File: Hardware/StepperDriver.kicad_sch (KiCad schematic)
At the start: 59 parts, among them J1 DC, J2 MOTOR, J3 OLED, J4 JTAG, SW1 SPST_TS, SW2 SPST_TS, SW3 SPST_TS, U1 TPS5430DDA, U2 TMC2208-LA, U3 XIAO-ESP32C6

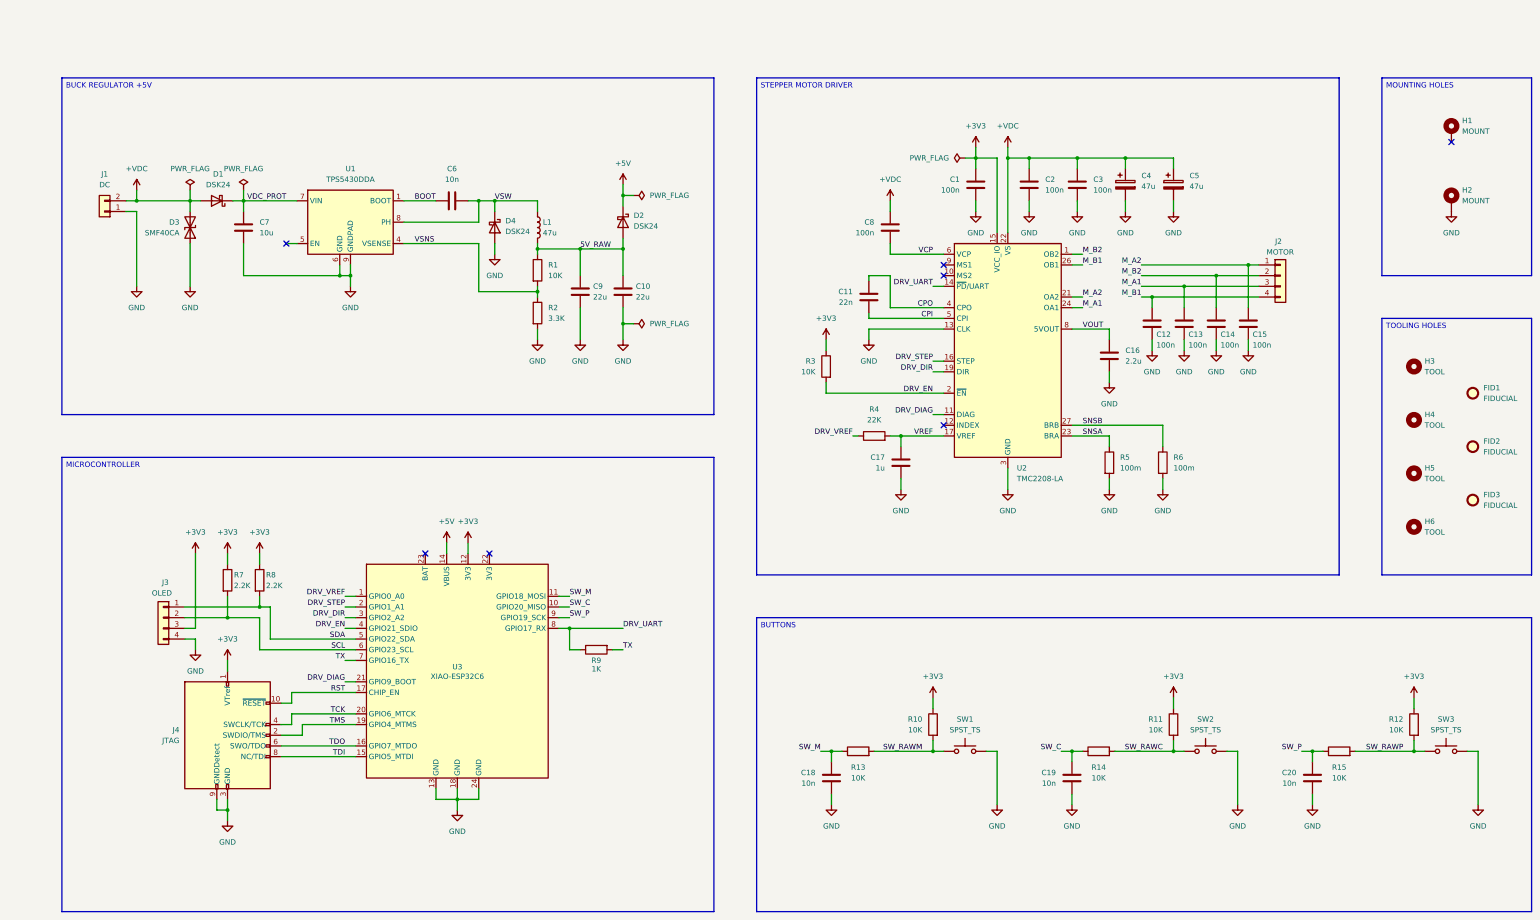
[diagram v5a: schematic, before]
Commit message: Driver update
Moved to the better TMC2209 stepper motor driver.
Added a status LED for the voltage regulator.
Updated the output files.
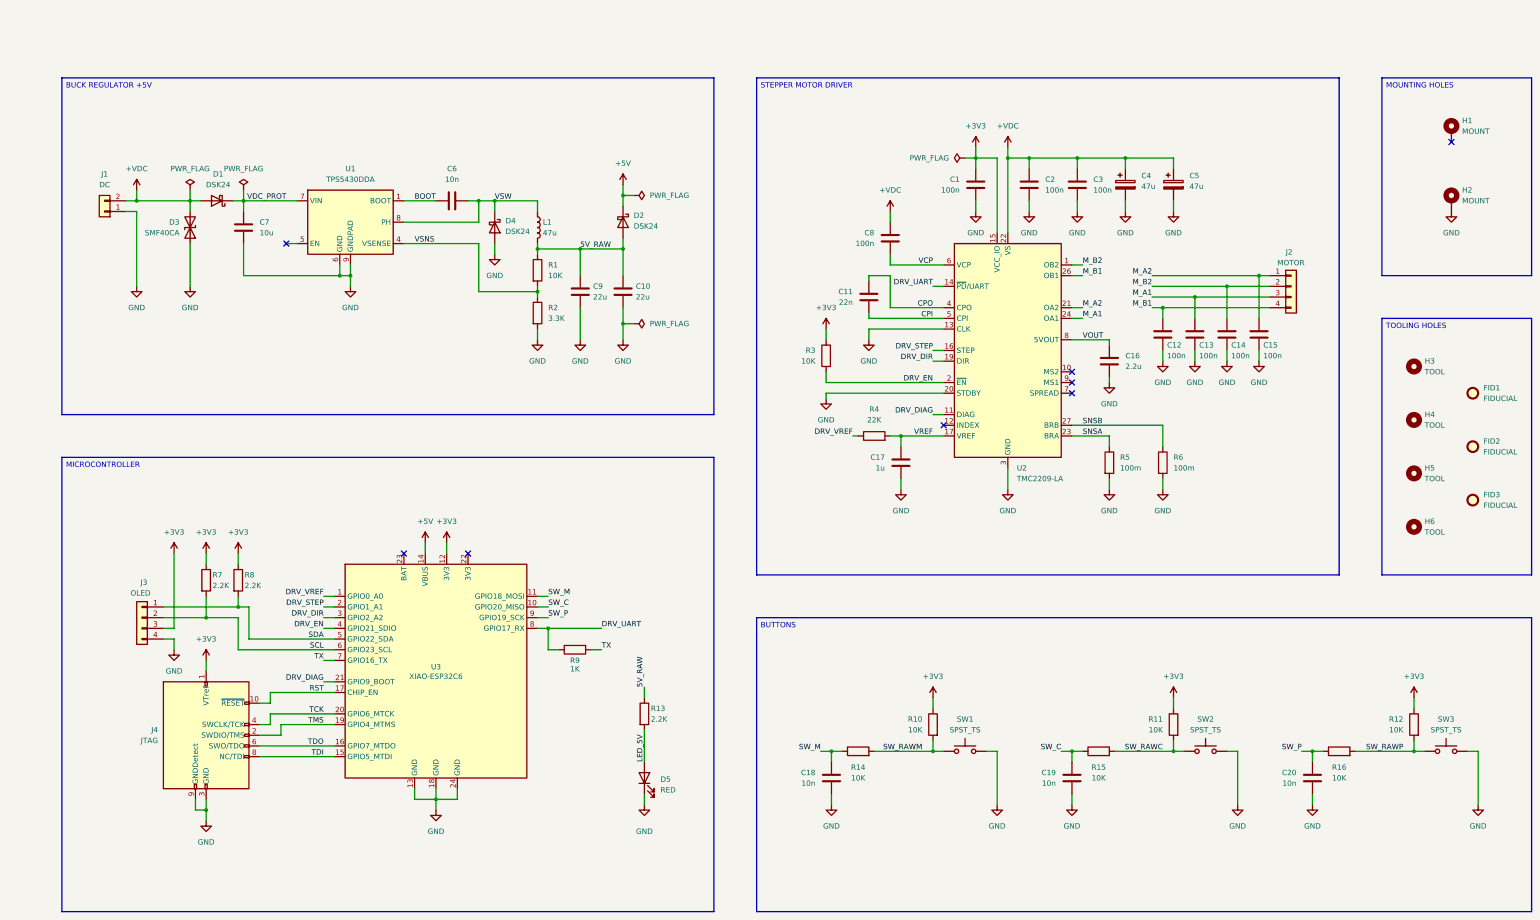
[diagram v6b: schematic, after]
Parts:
- removed U2: TMC2208-LA, Custom_Parts:QFN-28-1EP_5x5mm_P0.5mm_EP3.1x3.1mm_ThermalVias, symbol Driver_Motor:TMC2208-LA
- added D5: RED, LED_SMD:LED_0603_1608Metric, symbol Device:LED
- added R13: 2.2K, Resistor_SMD:R_0603_1608Metric, symbol Device:R
- added U2: TMC2209-LA, Custom_Parts:VQFN-28-1EP_5x5mm_P0.5mm_EP3.7x3.7mm_ThermalVias, symbol Custom_Parts:TMC2209-LA
- renumbered R13 to R14, R14 to R15, R15 to R16
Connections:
- net +3V3: now also U2.15 (VCC_IO)
- net +VDC: now also U2.22 (VS), U2.28 (VS)
- net 5V_RAW: now also R13.1
- net CPI: now also U2.5 (CPI)
- net CPO: now also U2.4 (CPO)
- net DRV_DIAG: now also U2.11 (DIAG)
- net DRV_DIR: now also U2.19 (DIR)
- net DRV_EN: now also U2.2 (~{EN})
- net DRV_STEP: now also U2.16 (STEP)
- net DRV_UART: now also U2.14 (~{PD}/UART)
- net GND: now also D5.1 (K), U2.13 (CLK), U2.18 (GND), U2.20 (STDBY), U2.29 (GND), U2.3 (GND)
- net M_A1: now also U2.24 (OA1)
- net M_A2: now also U2.21 (OA2)
- net M_B1: now also U2.26 (OB1)
- net M_B2: now also U2.1 (OB2)
- net SNSA: now also U2.23 (BRA)
- net SNSB: now also U2.27 (BRB)
- net VCP: now also U2.6 (VCP)
- net VOUT: now also U2.8 (5VOUT)
- net VREF: now also U2.17 (VREF)
- new net LED_5V: D5.2 (A), R13.2
- no-connect marks 7 -> 8
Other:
- moved on the sheet: C12, C13, C14, C15, C16, C8, J2, J3, J4, R3, R7, R8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

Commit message: Output files
Minor changes on the PCB.
Updated the bulk capacitors for the board to have a lower voltage rating.
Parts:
- C4, C5: footprint Capacitor_SMD:CP_Elec_6.3x5.4 -> Capacitor_SMD:CP_Elec_6.3x5.8; JLCPCB Part C44606723 -> C5246552; Manufacturer Part SM476M050E0800 -> HV1V476M0605PZ
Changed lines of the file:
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@@
 			)
 		)
-		(property "Footprint" "Capacitor_SMD:CP_Elec_6.3x5.4"
+		(property "Footprint" "Capacitor_SMD:CP_Elec_6.3x5.8"
 			(at 286.7152 66.04 0)
 			(hide yes)
@@
 			)
 		)
-		(property "JLCPCB Part" "C44606723"
+		(property "JLCPCB Part" "C5246552"
 			(at 285.75 62.23 0)
 			(hide yes)
@@
 			)
 		)
-		(property "Manufacturer Part" "SM476M050E0800"
+		(property "Manufacturer Part" "HV1V476M0605PZ"
 			(at 285.75 62.23 0)
 			(hide yes)
@@
 			)
 		)
-		(property "Footprint" "Capacitor_SMD:CP_Elec_6.3x5.4"
+		(property "Footprint" "Capacitor_SMD:CP_Elec_6.3x5.8"
 			(at 298.1452 66.04 0)
 			(hide yes)
@@
 			)
 		)
-		(property "JLCPCB Part" "C44606723"
+		(property "JLCPCB Part" "C5246552"
 			(at 297.18 62.23 0)
 			(hide yes)
@@
 			)
 		)
-		(property "Manufacturer Part" "SM476M050E0800"
+		(property "Manufacturer Part" "HV1V476M0605PZ"
 			(at 297.18 62.23 0)
 			(hide yes)

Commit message: Output files
Minor changes to the board and schematic.
Updated the output files.
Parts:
- removed H4: TOOL, MountingHole:ToolingHole_1.152mm, symbol Mechanical:MountingHole
- R9: value 1K -> 0R; JLCPCB Part C21190 -> C21189; Manufacturer Part 0603WAF1001T5E -> 0603WAF0000T5E
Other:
- moved on the sheet: FID1, FID3, H3, H5, H6
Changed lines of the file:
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@@
 	(symbol
 		(lib_id "Mechanical:MountingHole")
-		(at 354.33 130.81 0)
+		(at 354.33 124.46 0)
 		(unit 1)
 		(body_style 1)
@@
 		(fields_autoplaced yes)
 		(property "Reference" "H5"
-			(at 356.87 129.5399 0)
+			(at 356.87 123.1899 0)
 			(show_name no)
 			(do_not_autoplace no)
@@
 		)
 		(property "Value" "TOOL"
-			(at 356.87 132.0799 0)
+			(at 356.87 125.7299 0)
 			(show_name no)
 			(do_not_autoplace no)
@@
 		)
 		(property "Footprint" "MountingHole:ToolingHole_1.152mm"
-			(at 354.33 130.81 0)
+			(at 354.33 124.46 0)
 			(hide yes)
 			(show_name no)
@@
 		)
 		(property "Datasheet" ""
-			(at 354.33 130.81 0)
+			(at 354.33 124.46 0)
 			(hide yes)
 			(show_name no)
@@
 		)
 		(property "Description" "Mounting Hole without connection"
-			(at 354.33 130.81 0)
+			(at 354.33 124.46 0)
 			(hide yes)
 			(show_name no)
@@
 		)
 		(property "JLCPCB Part" "-"
-			(at 354.33 130.81 0)
+			(at 354.33 124.46 0)
 			(hide yes)
 			(show_name no)
@@
 		)
 		(property "Manufacturer Part" "-"
-			(at 354.33 130.81 0)
+			(at 354.33 124.46 0)
 			(hide yes)
 			(show_name no)
@@
 	(symbol
 		(lib_id "Mechanical:MountingHole")
-		(at 354.33 105.41 0)
+		(at 354.33 107.95 0)
 		(unit 1)
 		(body_style 1)
@@
 		(fields_autoplaced yes)
 		(property "Reference" "H3"
-			(at 356.87 104.1399 0)
-			(show_name no)
-			(do_not_autoplace no)
-			(effects
-				(font
-					(size 1.27 1.27)
-				)
-				(justify left)
-			)
-		)
-		(property "Value" "TOOL"
 			(at 356.87 106.6799 0)
 			(show_name no)
@@
 			)
 		)
-		(property "Footprint" "MountingHole:ToolingHole_1.152mm"
-			(at 354.33 105.41 0)
-			(hide yes)
-			(show_name no)
-			(do_not_autoplace no)
-			(effects
-				(font
-					(size 1.27 1.27)
-				)
-			)
-		)
-		(property "Datasheet" ""
-			(at 354.33 105.41 0)
-			(hide yes)
-			(show_name no)
-			(do_not_autoplace no)
-			(effects
-				(font
-					(size 1.27 1.27)
-				)
-			)
-		)
-		(property "Description" "Mounting Hole without connection"
-			(at 354.33 105.41 0)
-			(hide yes)
-			(show_name no)
-			(do_not_autoplace no)
-			(effects
-				(font
-					(size 1.27 1.27)
-				)
-			)
-		)
-		(property "JLCPCB Part" "-"
-			(at 354.33 105.41 0)
-			(hide yes)
-			(show_name no)
-			(do_not_autoplace no)
-			(effects
-				(font
-					(size 1.27 1.27)
-				)
-			)
-		)
-		(property "Manufacturer Part" "-"
-			(at 354.33 105.41 0)
-			(hide yes)
-			(show_name no)
-			(do_not_autoplace no)
-			(effects
-				(font
-					(size 1.27 1.27)
-				)
-			)
-		)
-		(instances
-			(project "StepperDriver"
-				(path "/f5ca4343-daa3-43f5-9432-f92f223fbf4e"
-					(reference "H3")
-					(unit 1)
-				)
-			)
-		)
-	)
-	(symbol
-		(lib_id "Mechanical:MountingHole")
-		(at 354.33 118.11 0)
-		(unit 1)
-		(body_style 1)
-		(exclude_from_sim no)
-		(in_bom no)
-		(on_board yes)
-		(in_pos_files yes)
-		(dnp no)
-		(fields_autoplaced yes)
-		(property "Reference" "H4"
-			(at 356.87 116.8399 0)
-			(show_name no)
-			(do_not_autoplace no)
-			(effects
-				(font
-					(size 1.27 1.27)
-				)
-				(justify left)
-			)
-		)
 		(property "Value" "TOOL"
-			(at 356.87 119.3799 0)
+			(at 356.87 109.2199 0)
 			(show_name no)
 			(do_not_autoplace no)
@@
 		)
 		(property "Footprint" "MountingHole:ToolingHole_1.152mm"
-			(at 354.33 118.11 0)
+			(at 354.33 107.95 0)
 			(hide yes)
 			(show_name no)
@@
 		)
 		(property "Datasheet" ""
-			(at 354.33 118.11 0)
+			(at 354.33 107.95 0)
 			(hide yes)
 			(show_name no)
@@
 		)
 		(property "Description" "Mounting Hole without connection"
-			(at 354.33 118.11 0)
+			(at 354.33 107.95 0)
 			(hide yes)
 			(show_name no)
@@
 		)
 		(property "JLCPCB Part" "-"
-			(at 354.33 118.11 0)
+			(at 354.33 107.95 0)
 			(hide yes)
 			(show_name no)
@@
 		)
 		(property "Manufacturer Part" "-"
-			(at 354.33 118.11 0)
+			(at 354.33 107.95 0)
 			(hide yes)
 			(show_name no)
@@
 			(project "StepperDriver"
 				(path "/f5ca4343-daa3-43f5-9432-f92f223fbf4e"
-					(reference "H4")
+					(reference "H3")
 					(unit 1)
 				)
@@
 			)
 		)
-		(property "Value" "1K"
+		(property "Value" "0R"
 			(at 154.94 177.292 90)
 			(show_name no)
@@
 			)
 		)
-		(property "JLCPCB Part" "C21190"
+		(property "JLCPCB Part" "C21189"
 			(at 154.94 172.72 90)
 			(hide yes)
@@
 			)
 		)
-		(property "Manufacturer Part" "0603WAF1001T5E"
+		(property "Manufacturer Part" "0603WAF0000T5E"
 			(at 154.94 172.72 90)
 			(hide yes)
@@
 	(symbol
 		(lib_id "Mechanical:Fiducial")
-		(at 368.3 137.16 0)
+		(at 368.3 140.97 0)
 		(unit 1)
 		(body_style 1)
@@
 		(fields_autoplaced yes)
 		(property "Reference" "FID3"
-			(at 370.84 135.8899 0)
+			(at 370.84 139.6999 0)
 			(show_name no)
 			(do_not_autoplace no)
@@
 		)
 		(property "Value" "FIDUCIAL"
-			(at 370.84 138.4299 0)
+			(at 370.84 142.2399 0)
 			(show_name no)
 			(do_not_autoplace no)
@@
 		)
 		(property "Footprint" "Fiducial:Fiducial_0.75mm_Mask1.5mm"
-			(at 368.3 137.16 0)
+			(at 368.3 140.97 0)
 			(hide yes)
 			(show_name no)
@@
 		)
 		(property "Datasheet" ""
-			(at 368.3 137.16 0)
+			(at 368.3 140.97 0)
 			(hide yes)
 			(show_name no)
@@
 		)
 		(property "Description" "Fiducial Marker"
-			(at 368.3 137.16 0)
+			(at 368.3 140.97 0)
 			(hide yes)
 			(show_name no)
@@
 		)
 		(property "JLCPCB Part" "-"
-			(at 368.3 137.16 0)
+			(at 368.3 140.97 0)
 			(hide yes)
 			(show_name no)
@@
 		)
 		(property "Manufacturer Part" "-"
-			(at 368.3 137.16 0)
+			(at 368.3 140.97 0)
 			(hide yes)
 			(show_name no)
@@
 	(symbol
 		(lib_id "Mechanical:Fiducial")
-		(at 368.3 111.76 0)
+		(at 368.3 107.95 0)
 		(unit 1)
 		(body_style 1)
@@
 		(fields_autoplaced yes)
 		(property "Reference" "FID1"
-			(at 370.84 110.4899 0)
+			(at 370.84 106.6799 0)
 			(show_name no)
 			(do_not_autoplace no)
@@
 		)
 		(property "Value" "FIDUCIAL"
-			(at 370.84 113.0299 0)
+			(at 370.84 109.2199 0)
 			(show_name no)
 			(do_not_autoplace no)
@@
 		)
 		(property "Footprint" "Fiducial:Fiducial_0.75mm_Mask1.5mm"
-			(at 368.3 111.76 0)
+			(at 368.3 107.95 0)
 			(hide yes)
 			(show_name no)
@@
 		)
 		(property "Datasheet" ""
-			(at 368.3 111.76 0)
+			(at 368.3 107.95 0)
 			(hide yes)
 			(show_name no)
@@
 		)
 		(property "Description" "Fiducial Marker"
-			(at 368.3 111.76 0)
+			(at 368.3 107.95 0)
 			(hide yes)
 			(show_name no)
@@
 		)
 		(property "JLCPCB Part" "-"
-			(at 368.3 111.76 0)
+			(at 368.3 107.95 0)
 			(hide yes)
 			(show_name no)
@@
 		)
 		(property "Manufacturer Part" "-"
-			(at 368.3 111.76 0)
+			(at 368.3 107.95 0)
 			(hide yes)
 			(show_name no)
@@
 	(symbol
 		(lib_id "Mechanical:MountingHole")
-		(at 354.33 143.51 0)
+		(at 354.33 140.97 0)
 		(unit 1)
 		(body_style 1)
@@
 		(fields_autoplaced yes)
 		(property "Reference" "H6"
-			(at 356.87 142.2399 0)
+			(at 356.87 139.6999 0)
 			(show_name no)
 			(do_not_autoplace no)
@@
 		)
 		(property "Value" "TOOL"
-			(at 356.87 144.7799 0)
+			(at 356.87 142.2399 0)
 			(show_name no)
 			(do_not_autoplace no)
@@
 		)
 		(property "Footprint" "MountingHole:ToolingHole_1.152mm"
-			(at 354.33 143.51 0)
+			(at 354.33 140.97 0)
 			(hide yes)
 			(show_name no)
@@
 		)
 		(property "Datasheet" ""
-			(at 354.33 143.51 0)
+			(at 354.33 140.97 0)
 			(hide yes)
 			(show_name no)
@@
 		)
 		(property "Description" "Mounting Hole without connection"
-			(at 354.33 143.51 0)
+			(at 354.33 140.97 0)
 			(hide yes)
 			(show_name no)
@@
 		)
 		(property "JLCPCB Part" "-"
-			(at 354.33 143.51 0)
+			(at 354.33 140.97 0)
 			(hide yes)
 			(show_name no)
@@
 		)
 		(property "Manufacturer Part" "-"
-			(at 354.33 143.51 0)
+			(at 354.33 140.97 0)
 			(hide yes)
 			(show_name no)
